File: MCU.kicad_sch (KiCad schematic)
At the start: 40 parts, among them J15 Conn_01x08, J16 Conn_02x04_Odd_Even, J17 Conn_01x04, J19 Conn_01x04, SW1 SW_Push_Dual, SW2 SW_Push_Dual, SW3 SW_DIP_x08, U15 MCP1700-3302E_SOT23, U17 MCP2562FD, U18 W25Q256JV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

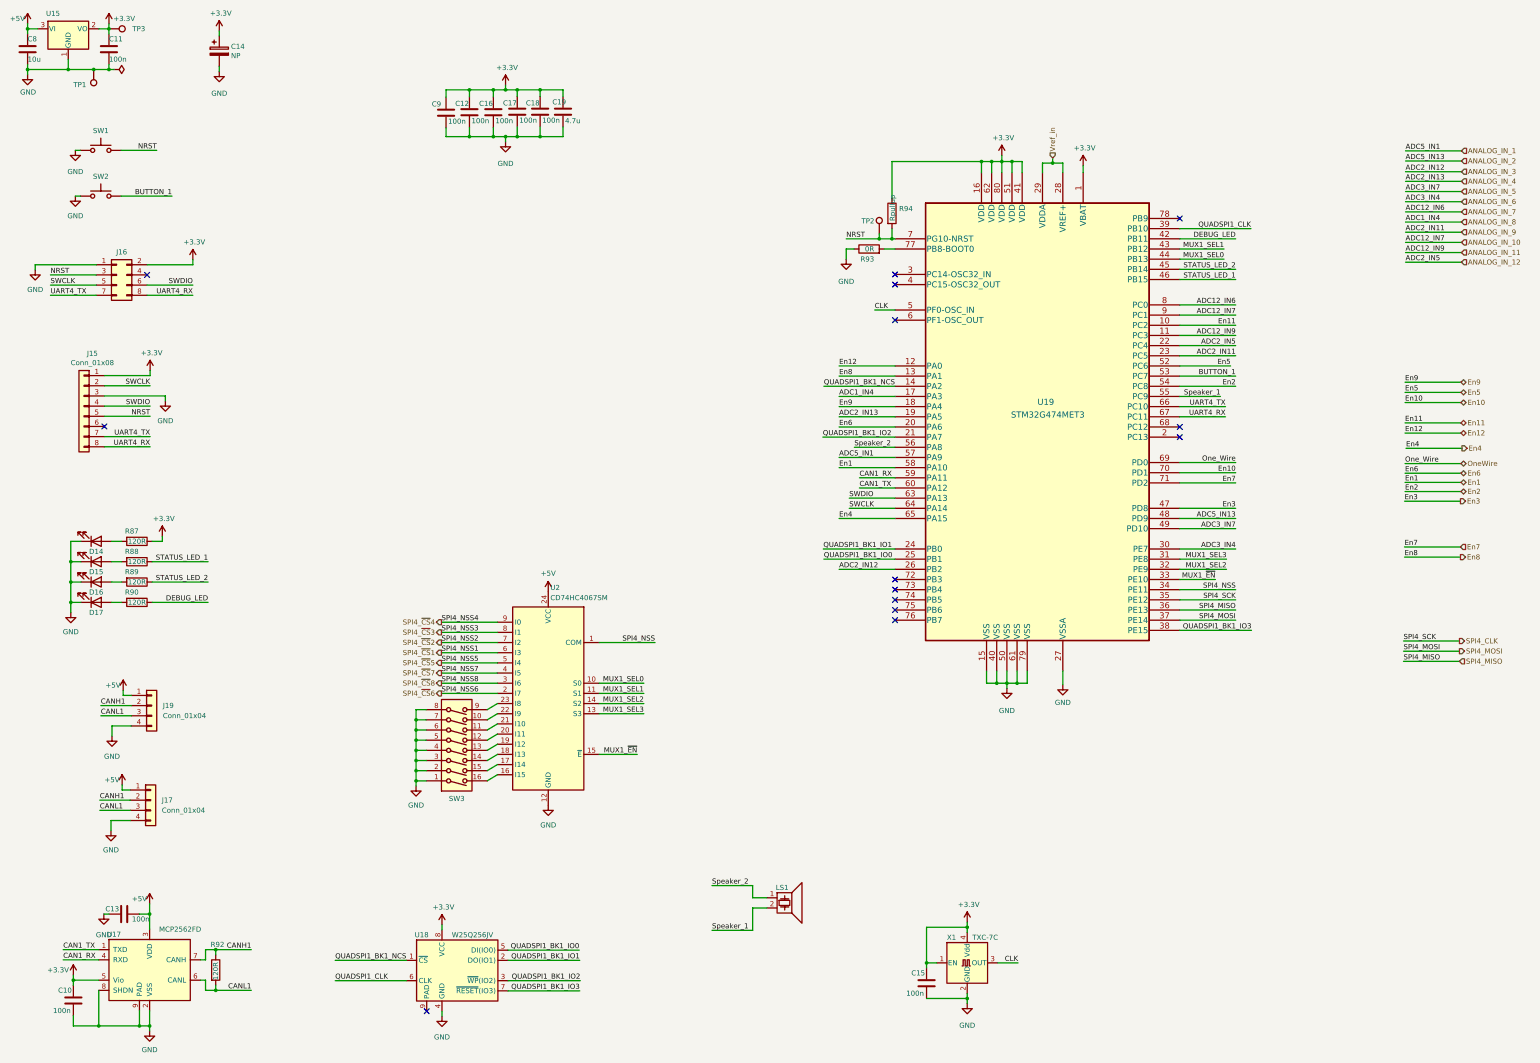
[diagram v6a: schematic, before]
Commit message: Circuit fix
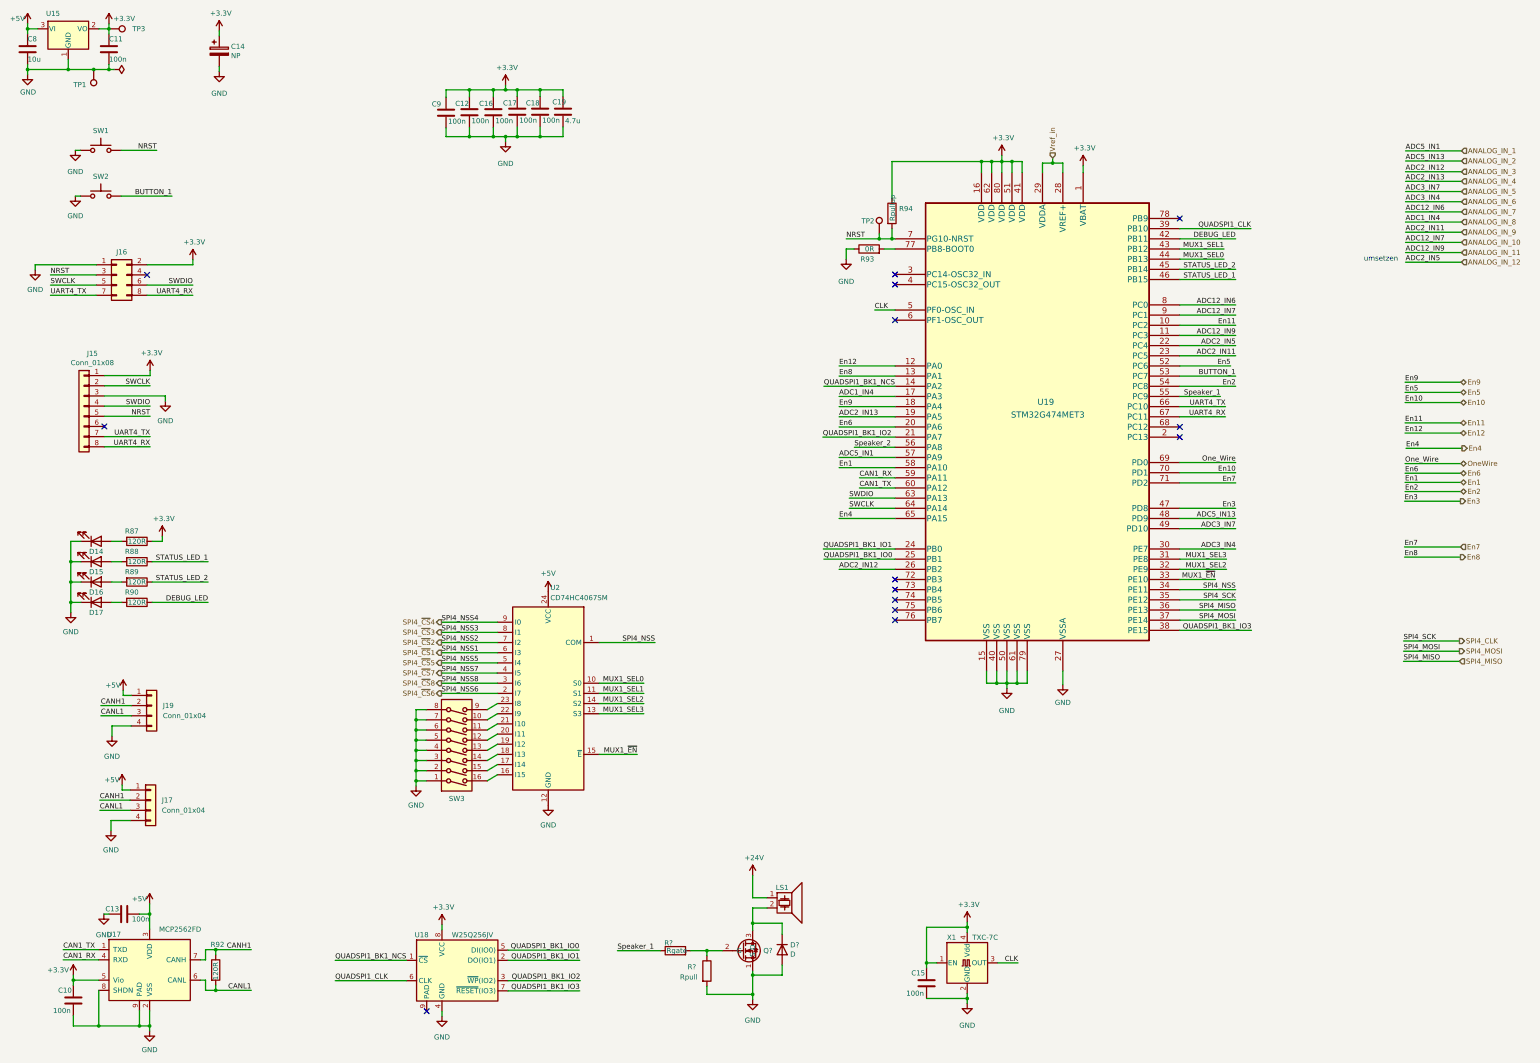
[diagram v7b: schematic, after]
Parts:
- added D?: D, Diode_SMD:D_SOD-123F, symbol Device:D
- added Q?: BSZ0902NSATMA1, TXV_Library_Footprints:PG_TSDSON-8, symbol TXV_Library_Symbols:BSZ0902NSATMA1
- added R?: Rpull, Resistor_SMD:R_0603_1608Metric, symbol Device:R
- added R?: Rgate, Resistor_SMD:R_0603_1608Metric, symbol Device:R
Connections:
- net GND: now also D?.2 (A), Q?.1 (S), R?.2
- net Speaker_1: now also R?.1; no longer LS1.2
- net Speaker_2: no longer LS1.1
- new net: D?.1 (K), LS1.2, Q?.3 (D)
- new net: Q?.2 (G), R?.1, R?.2
- new net +24V: LS1.1
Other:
- note added: "umsetzen"

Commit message: Annotation fix
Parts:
- gave numbers to parts that had none: 4
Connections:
- net ANALOG_IN_12 renamed ANALOG_IN_0
- net En12 renamed En0
- net Speaker_2: no longer names the net of U19.56 (PA8)
- no-connect marks 14 -> 15
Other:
- moved on the sheet: D18, LS1, Q13, R73, R74, SW3, U2
